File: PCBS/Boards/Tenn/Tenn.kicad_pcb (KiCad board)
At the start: 2 copper layers, 34 parts, among them J1 Conn_01x02_Socket, J10 Conn_01x03_Male, J11 Conn_01x03_Male, J12 Conn_01x04_Female, J13 Conn_01x03_Male, J14 Conn_01x03_Male, J15 Conn_01x03_Male, J16 Conn_01x02_Male, J17 Conn_01x02_Male, J2 Conn_01x03_Male, J3 Conn_01x03_Male, J4 Conn_01x03_Male, J5 Conn_01x03_Male, J6 Conn_01x03_Male, J7 Conn_01x03_Male, J8 Conn_01x03_Male, J9 Conn_01x03_Male, SW2 SW_Push, SW3 SW_Push, SW4 SW_SPDT, U1 L7805, U2 DRV8871DDA, U3 DRV8871DDA

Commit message: updated README
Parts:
- J12: footprint Connector_PinHeader_2.54mm:PinHeader_1x04_P2.54mm_Vertical -> Connector_PinSocket_2.54mm:PinSocket_1x04_P2.54mm_Vertical
- J16, J17: footprint Connector_PinSocket_2.54mm:PinSocket_1x02_P2.54mm_Vertical -> Connector_JST:JST_XH_B2B-XH-A_1x02_P2.50mm_Vertical
- moved J2 91.1 mm to (192.8, 91.2), turned to -90 degrees
- moved J6 81.7 mm to (201.5, 91.2), turned to -90 degrees
- moved A1 67.9 mm to (165.5, 109.8), turned to 90 degrees
- moved J14 62.2 mm to (186.3, 122.2)
- moved J7 61.0 mm to (184.1, 91.2), turned to -90 degrees
- moved J13 55.2 mm to (168.8, 120.5)
- moved C1 53.9 mm to (71.9, 112.3)
- moved C2 53.9 mm to (71.9, 115.3)
- moved C3 53.9 mm to (71.9, 118.3)
- moved C4 53.9 mm to (71.9, 121.4)
- moved C5 53.9 mm to (79.5, 113.8)
- moved C6 53.9 mm to (79.5, 119.6)
- moved R1 53.9 mm to (71.9, 124.3)
- moved R2 53.9 mm to (71.9, 127.3)
- moved R3 53.9 mm to (71.9, 130.2)
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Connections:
- A1 pad 21: SDA -> Sens6
- A1 pad 22: SCL -> Sens7
- A1 pad 23: Sens6 -> SDA
- A1 pad 24: Sens7 -> SCL
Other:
- board outline added: 90 x 25 mm

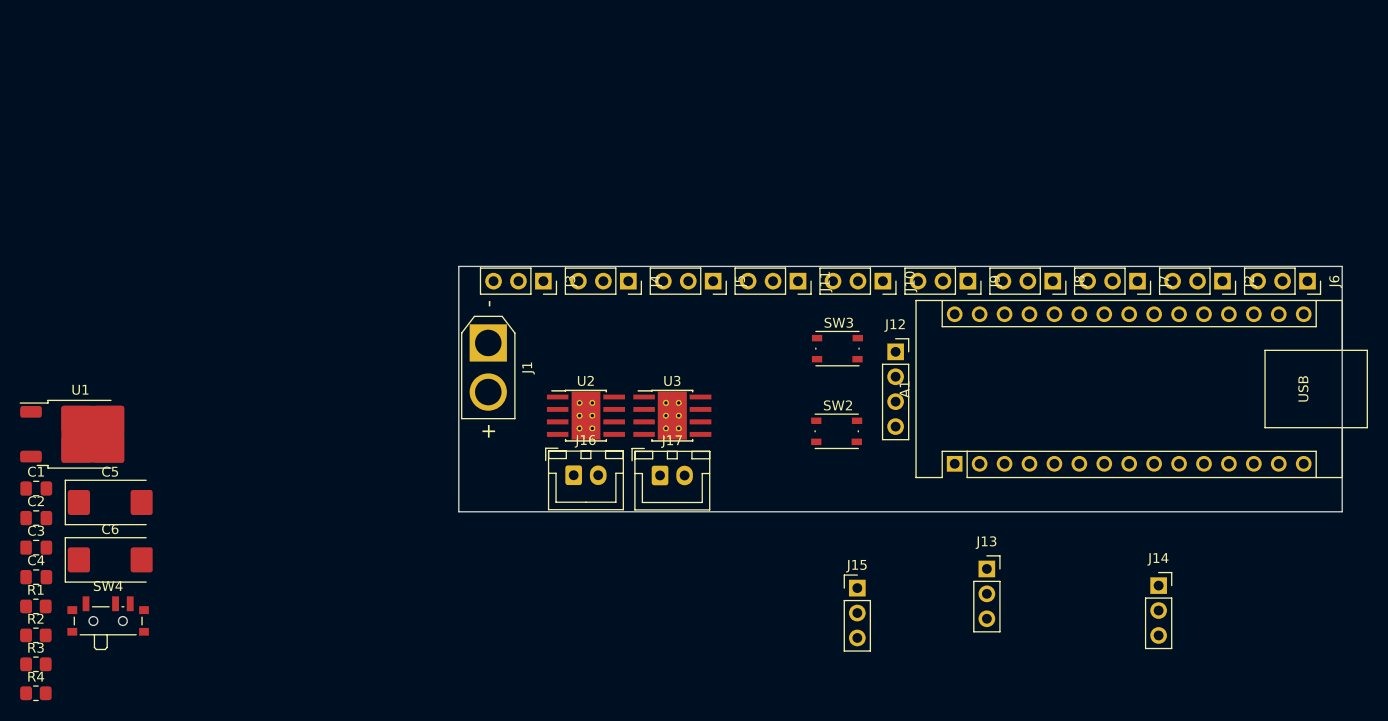
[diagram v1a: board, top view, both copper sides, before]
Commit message: updated Tei board PCB, all components now in place
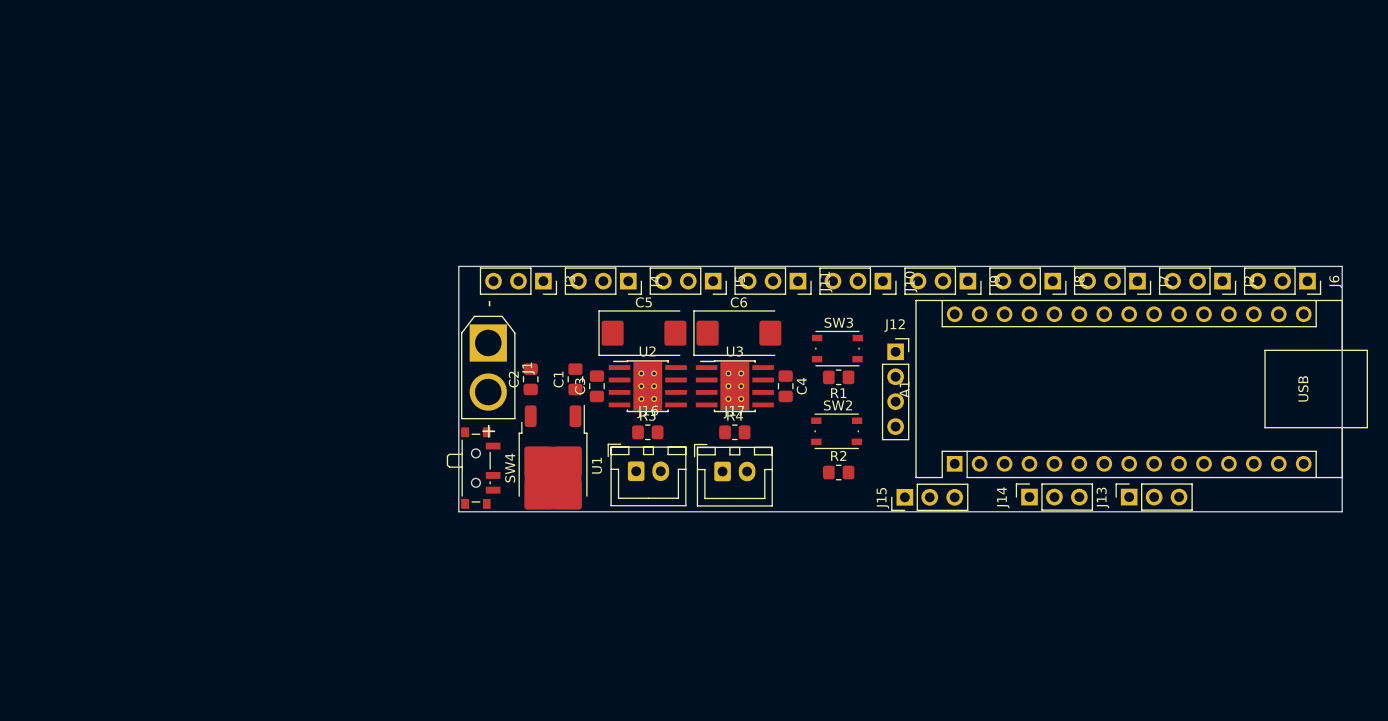
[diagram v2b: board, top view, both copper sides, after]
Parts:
- moved R1 85.1 mm to (153.7, 101.0), turned to 180 degrees
- moved R2 83.5 mm to (153.7, 110.7)
- moved C4 78.8 mm to (148.3, 101.9), turned to -90 degrees
- moved R4 76.0 mm to (143.1, 106.6)
- moved C6 68.1 mm to (143.5, 96.5)
- moved R3 66.7 mm to (134.2, 106.6)
- moved C3 59.4 mm to (129.1, 101.9), turned to 90 degrees
- moved C5 57.1 mm to (133.9, 96.5)
- moved C1 56.1 mm to (126.9, 101.2), turned to 90 degrees
- moved C2 52.3 mm to (122.3, 101.2), turned to 90 degrees
- moved U1 48.3 mm to (124.6, 110.0), turned to -90 degrees
- moved SW4 40.8 mm to (117.1, 110.2), turned to -90 degrees
- moved J13 16.2 mm to (183.3, 113.2), turned to 90 degrees
- moved J14 16.0 mm to (173.1, 113.2), turned to 90 degrees
- moved J15 10.4 mm to (160.4, 113.2), turned to 90 degrees
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
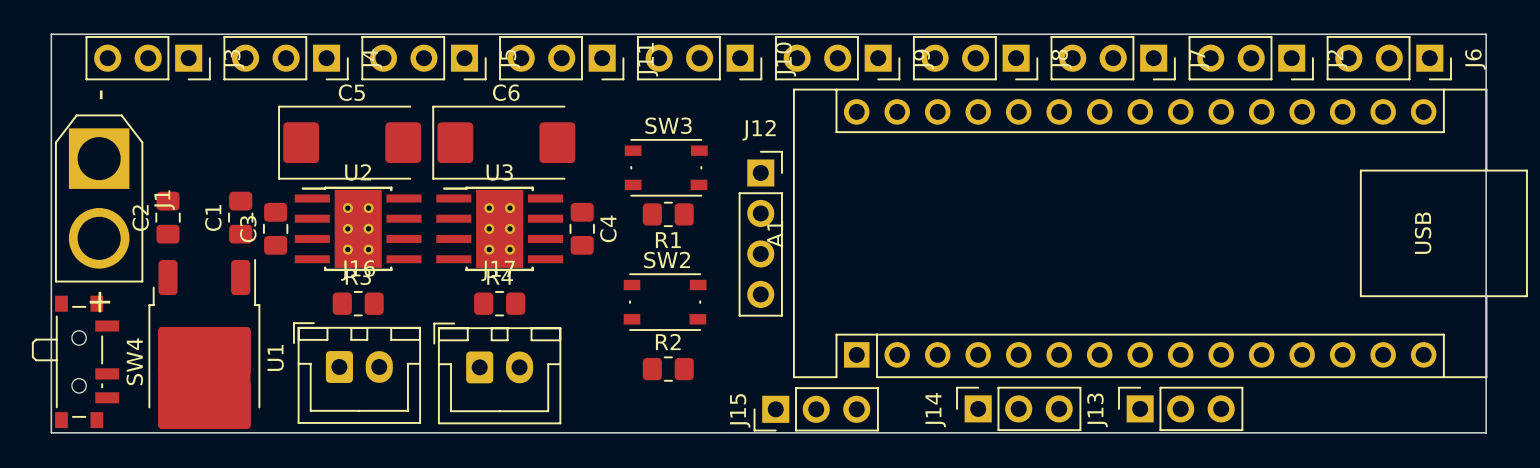
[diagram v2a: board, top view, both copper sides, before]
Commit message: Created Tamashi K1tsun3 in /code
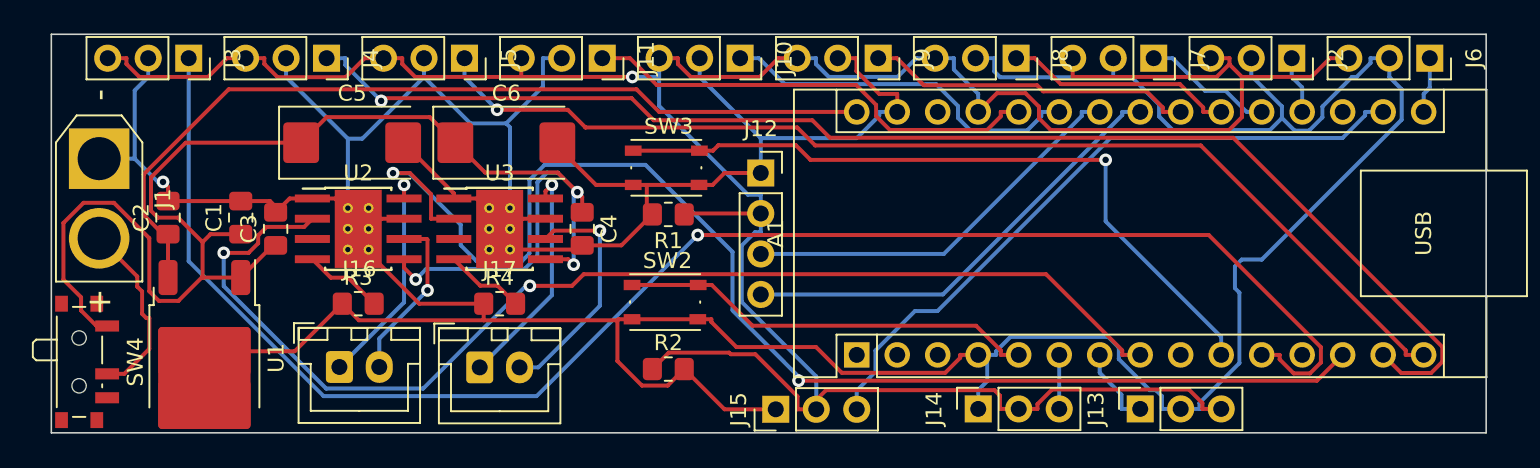
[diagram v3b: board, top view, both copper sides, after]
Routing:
- net GND: track 0.00 -> 310.3 mm, vias 0 -> 1
- net +5V: track 0.00 -> 180.3 mm, vias 0 -> 1
- net Sens0: track 0.00 -> 100.0 mm, vias 0 -> 1
- net VM: track 0.00 -> 94.7 mm, vias 0 -> 3
- net Sens1: track 0.00 -> 83.3 mm, vias 0 -> 1
- net MA1: track 0.00 -> 82.3 mm, vias 0 -> 2
- net MB1: track 0.00 -> 74.2 mm, vias 0 -> 2
- net Sens2: track 0.00 -> 68.7 mm, vias 0 -> 1
- net VCC: track 0.00 -> 54.8 mm
- net BTN2: track 0.00 -> 45.4 mm, vias 0 -> 1
- net +3.3V: track 0.00 -> 42.3 mm
- net Sens9: track 0.00 -> 29.0 mm
- net SDA: track 0.00 -> 28.7 mm
- net BTN1: track 0.00 -> 26.2 mm
- net SCL: track 0.00 -> 25.1 mm
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
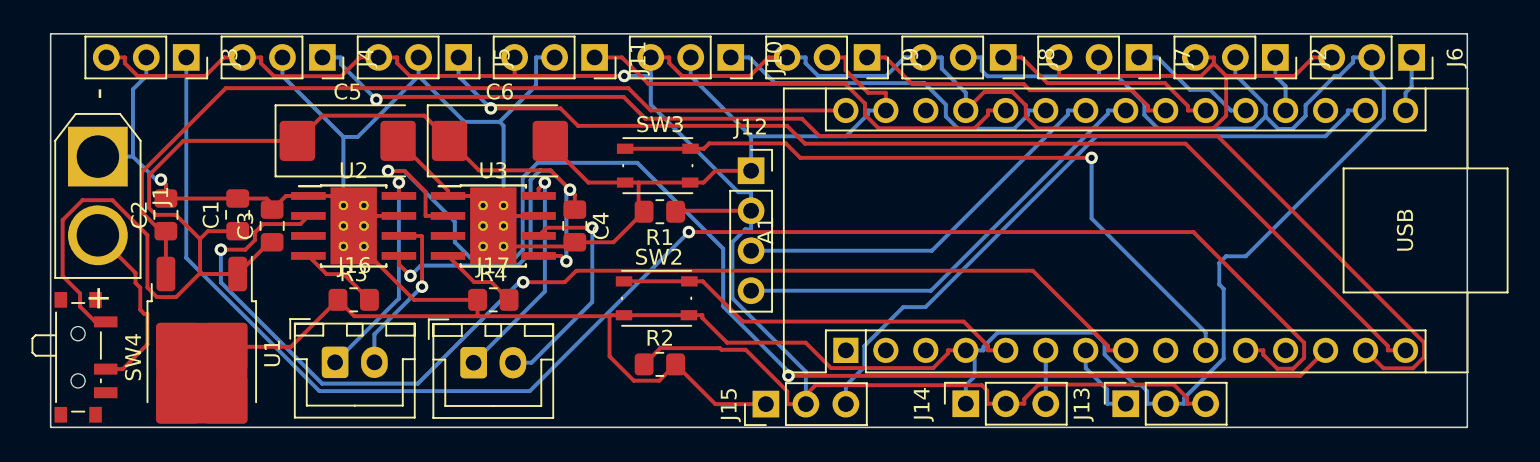
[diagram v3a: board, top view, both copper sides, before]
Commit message: Updates nets and adds tracks in pcb file
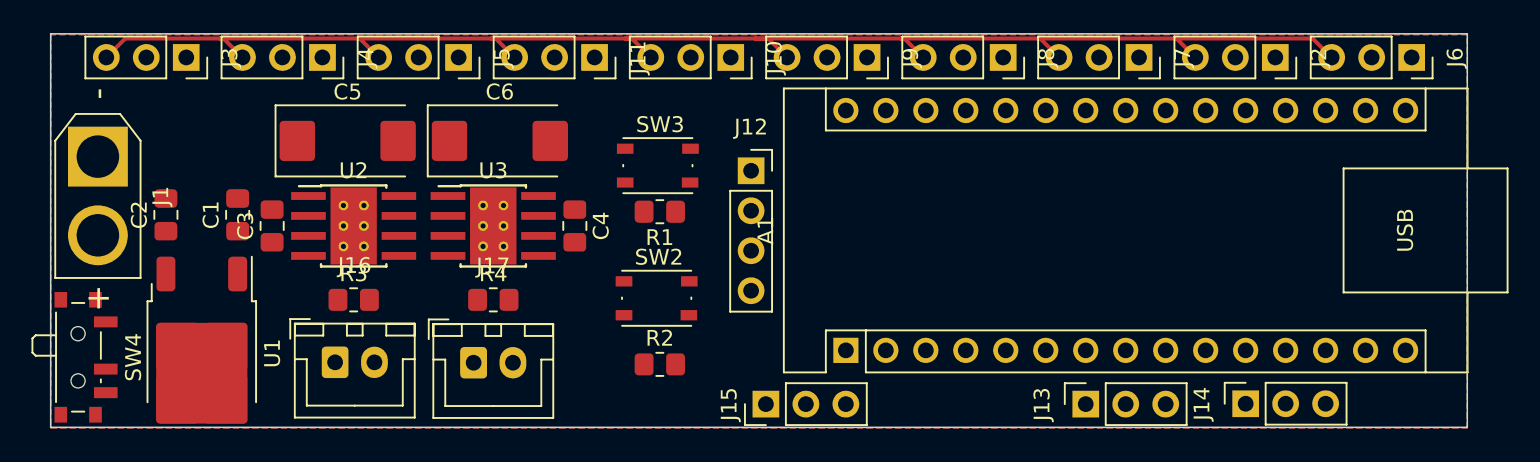
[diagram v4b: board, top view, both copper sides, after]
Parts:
- moved J14 17.8 mm to (190.9, 113.2)
- moved J13 2.54 mm to (180.8, 113.2)
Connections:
- A1 pad 12: MA2 -> Sens1
- A1 pad 13: MA1 -> Servo
- A1 pad 14: Sens1 -> MA1
- A1 pad 6: Servo -> MB1
- A1 pad 8: MB1 -> MB2
- A1 pad 9: MB2 -> MA2
- SW4 pad 1: VM -> Net-(J1-Pin_2)
- SW4 pad 2: Net-(J1-Pin_2) -> VM
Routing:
- net GND: track 310.3 -> 0.00 mm, vias 1 -> 0
- net Sens0: track 100.0 -> 0.00 mm, vias 1 -> 0
- net VM: track 94.7 -> 0.00 mm, vias 3 -> 0
- net +5V: track 180.3 -> 94.7 mm, vias 1 -> 0
- net Sens1: track 83.3 -> 0.00 mm, vias 1 -> 0
- net MA1: track 82.3 -> 0.00 mm, vias 2 -> 0
- net MB1: track 74.2 -> 0.00 mm, vias 2 -> 0
- net Sens2: track 68.7 -> 0.00 mm, vias 1 -> 0
- net VCC: track 54.8 -> 0.00 mm
- net BTN2: track 45.4 -> 0.00 mm, vias 1 -> 0
- net +3.3V: track 42.3 -> 0.00 mm
- net Sens9: track 29.0 -> 0.00 mm
- net SDA: track 28.7 -> 0.00 mm
- net BTN1: track 26.2 -> 0.00 mm
- net SCL: track 25.1 -> 0.00 mm
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- added copper zone on B.Cu, net GND
- added copper zone on F.Cu, net GND

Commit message: updates tenn PCB board, changes some connections and netclasses
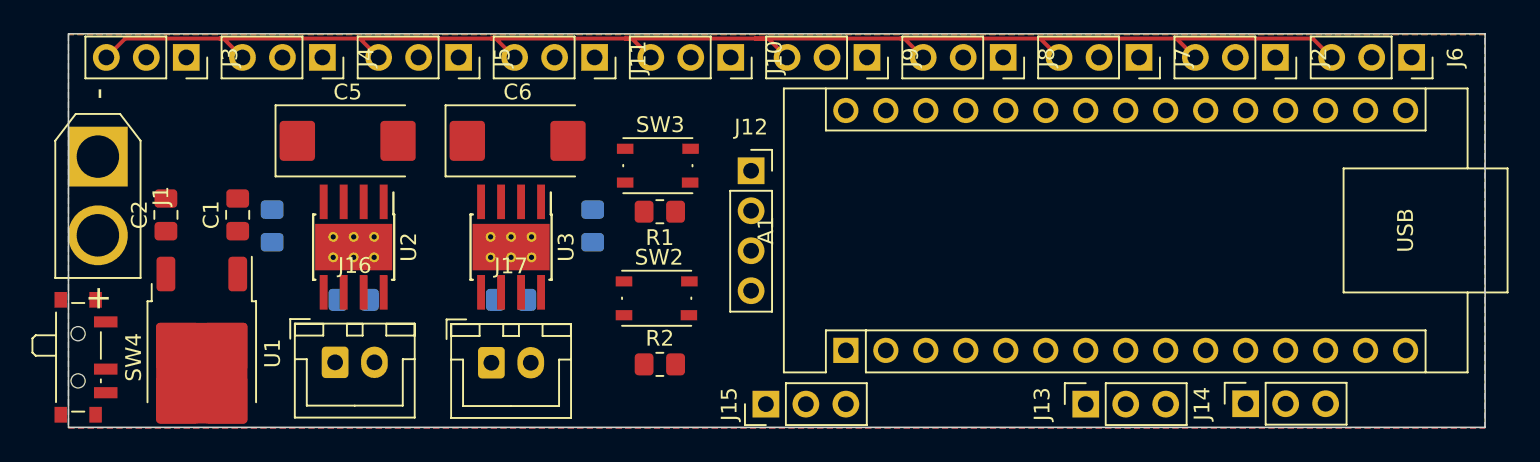
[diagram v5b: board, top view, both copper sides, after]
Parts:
- C3, C4, R3, R4: moved to B.Cu
- moved C3 20.4 mm to (149.4, 101.9)
- moved C4 19.2 mm to (129.1, 101.9)
- moved R3 10.0 mm to (144.2, 106.6), turned to 180 degrees
- moved R4 8.87 mm to (134.2, 106.6), turned to 180 degrees
- moved U3 1.76 mm to (144.2, 103.2), turned to -90 degrees
- moved U2 1.34 mm to (134.2, 103.2), turned to -90 degrees
- moved C6 1.13 mm to (144.7, 96.5)
- moved J17 1.13 mm to (143.0, 110.6)
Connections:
- U2 pad 6: Net-(J16-Pin_2) -> Net-(J16-Pin_1)
- U2 pad 8: Net-(J16-Pin_1) -> Net-(J16-Pin_2)
- U3 pad 6: Net-(J17-Pin_2) -> Net-(J17-Pin_1)
- U3 pad 8: Net-(J17-Pin_1) -> Net-(J17-Pin_2)

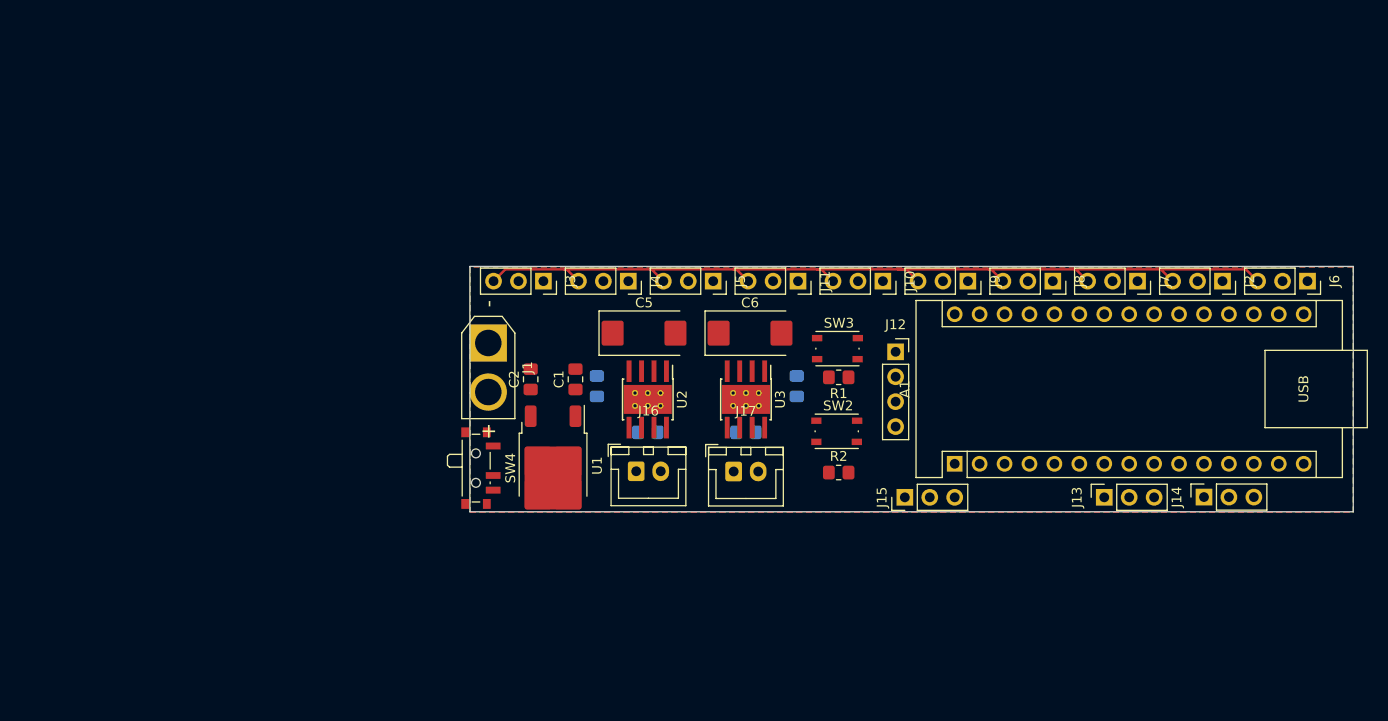
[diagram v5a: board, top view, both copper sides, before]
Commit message: updates the files in Tenn PCB board
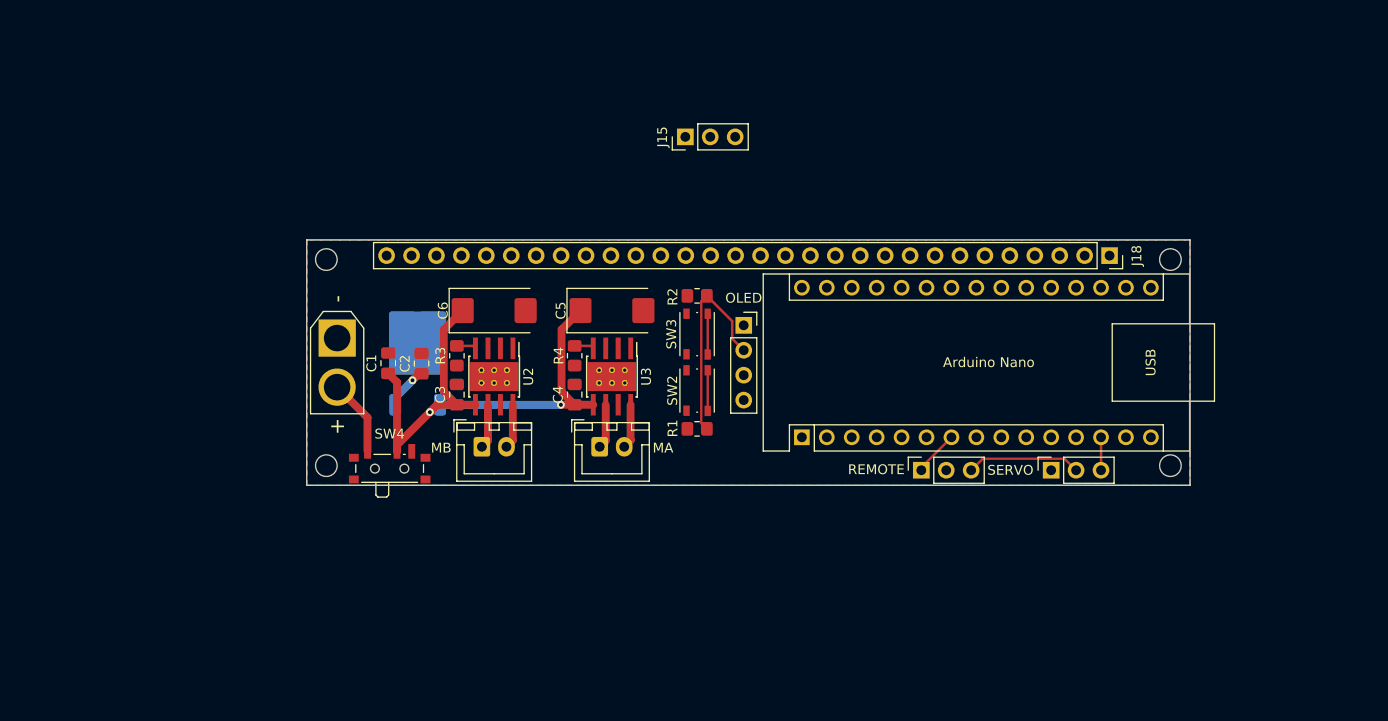
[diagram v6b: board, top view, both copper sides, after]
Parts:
- removed J10, J11, J2, J3, J4, J5, J6, J7, J8, J9: Conn_01x03_Male, Connector_PinSocket_2.54mm:PinSocket_1x03_P2.54mm_Vertical
- added J18: Conn_01x30_Pin, Connector_PinSocket_2.54mm:PinSocket_1x30_P2.54mm_Vertical, F.Cu at (181.3, 88.6)
- added REF**: MountingHole_2.2mm_M2_ISO7380, MountingHole:MountingHole_2.2mm_M2_ISO7380, F.Cu at (187.5, 89.0)
- added REF**: MountingHole_2.2mm_M2_ISO7380, MountingHole:MountingHole_2.2mm_M2_ISO7380, F.Cu at (101.5, 89.0)
- added REF**: MountingHole_2.2mm_M2_ISO7380, MountingHole:MountingHole_2.2mm_M2_ISO7380, F.Cu at (101.5, 110.0)
- added REF**: MountingHole_2.2mm_M2_ISO7380, MountingHole:MountingHole_2.2mm_M2_ISO7380, F.Cu at (187.5, 110.0)
- Arduino Nano: renamed from A1
- C3, C4, R3, R4: moved to F.Cu
- L7085/StepDownModule: renamed from U1; moved to B.Cu
- moved J15 43.0 mm to (138.1, 76.5)
- moved C3 34.6 mm to (114.8, 102.8)
- moved R3 30.5 mm to (114.8, 98.8), turned to 90 degrees
- moved C6 26.2 mm to (118.6, 94.2)
- moved R2 23.1 mm to (139.3, 92.7), turned to 180 degrees
- moved C1 19.2 mm to (107.8, 99.6)
- moved REMOTE 18.8 mm to (162.1, 110.5)
- moved L7085/StepDownModule 17.8 mm to (110.8, 98.8), turned to 90 degrees
- moved MB 15.9 mm to (117.3, 108.1)
- moved U2 15.8 mm to (118.6, 100.9)
- moved SERVO 15.8 mm to (175.3, 110.5)
- moved Arduino Nano 15.8 mm to (149.9, 107.1)
- moved OLED 15.7 mm to (144.0, 95.7)
- moved J1 15.4 mm to (102.6, 97.0)
- moved R1 15.4 mm to (139.3, 106.2)
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- renumbered J17 to MA, J16 to MB, J12 to OLED, J13 to REMOTE, J14 to SERVO
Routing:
- net +5V: track 94.7 -> 32.8 mm
- net VM: track 0.00 -> 57.8 mm, vias 0 -> 2
- net Net-(J1-Pin_2): track 0.00 -> 7.82 mm
- net GO: track 0.00 -> 4.63 mm
- net Net-(J17-Pin_2): track 0.00 -> 4.55 mm
- net Net-(J16-Pin_2): track 0.00 -> 4.55 mm
- net Net-(J17-Pin_1): track 0.00 -> 4.53 mm
- net Net-(J16-Pin_1): track 0.00 -> 4.53 mm
- net VCC: track 0.00 -> 4.43 mm, vias 0 -> 1
- net BTN2: track 0.00 -> 4.15 mm
- net BTN1: track 0.00 -> 4.15 mm
- net Servo: track 0.00 -> 3.36 mm
- net Net-(U3-ILIM): track 0.00 -> 2.00 mm
- net Net-(U2-ILIM): track 0.00 -> 2.00 mm
